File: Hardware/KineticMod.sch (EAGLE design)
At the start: 32 parts, among them P1 ALPS_RK09K_VERTICAL, P2 ALPS_RK09K_VERTICAL, P3 ALPS_RK09K_VERTICAL, P4 ALPS_RK09K_VERTICAL, Q1 AOD417, U1 PCA9685

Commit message: Updated KineticMod
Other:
- note added: "By J.G.Aguado"
- note added: "R2"
- note removed: "Designed by J.G.Aguado"
- note removed: "KineticMod"

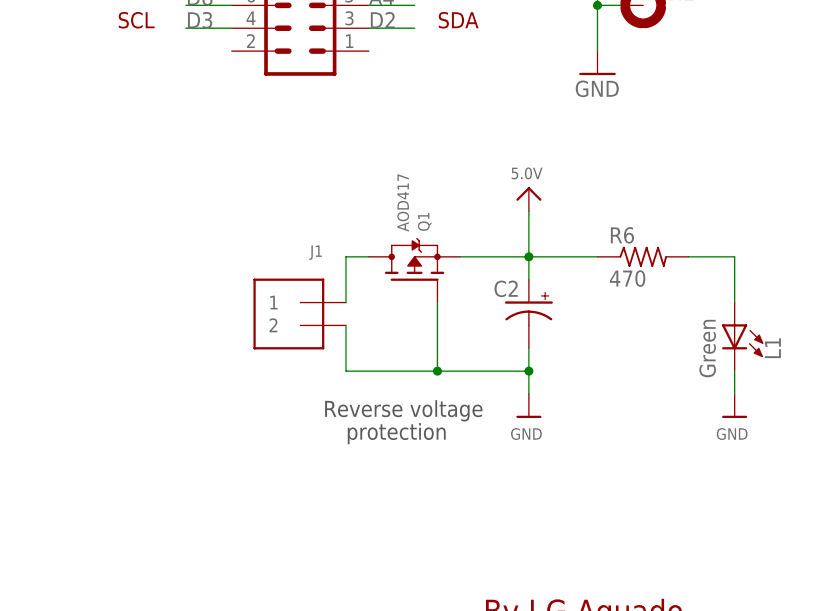
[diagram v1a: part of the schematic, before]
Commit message: Updated capacitors: - C2 replaced by 470uF 2917 (7343) - Added C3 470uF 2917 (7343)
Updated silkscreen
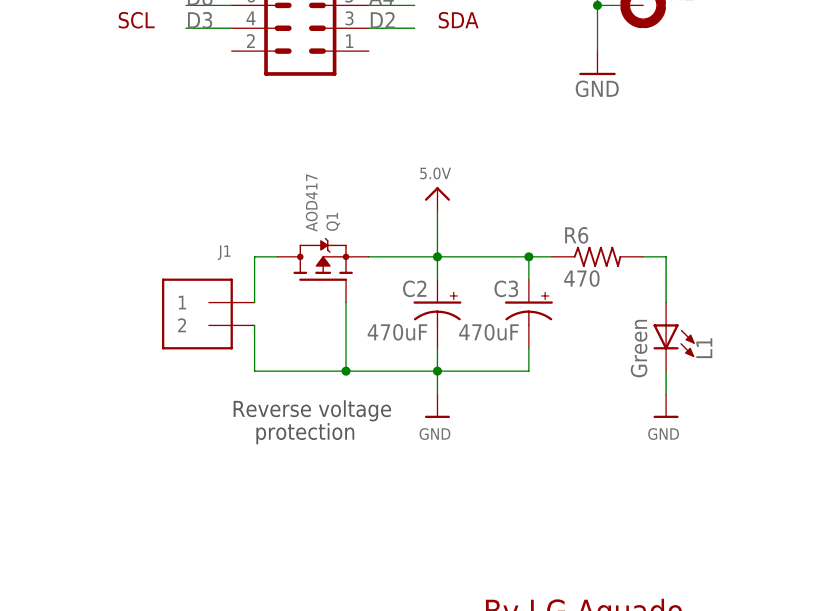
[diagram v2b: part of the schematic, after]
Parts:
- added C3: 470uF, rcl:CPOL-USD/7343-31R
- C2: value (none) -> 470uF; device SparkFun:CAP_POL7343 -> rcl:CPOL-USD/7343-31R
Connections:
- net 5.0V: now also C3.+
- net GND: now also C3.-
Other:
- moved on the sheet: C2, J1, L1, Q1, R6
